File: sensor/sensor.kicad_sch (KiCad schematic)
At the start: 17 parts

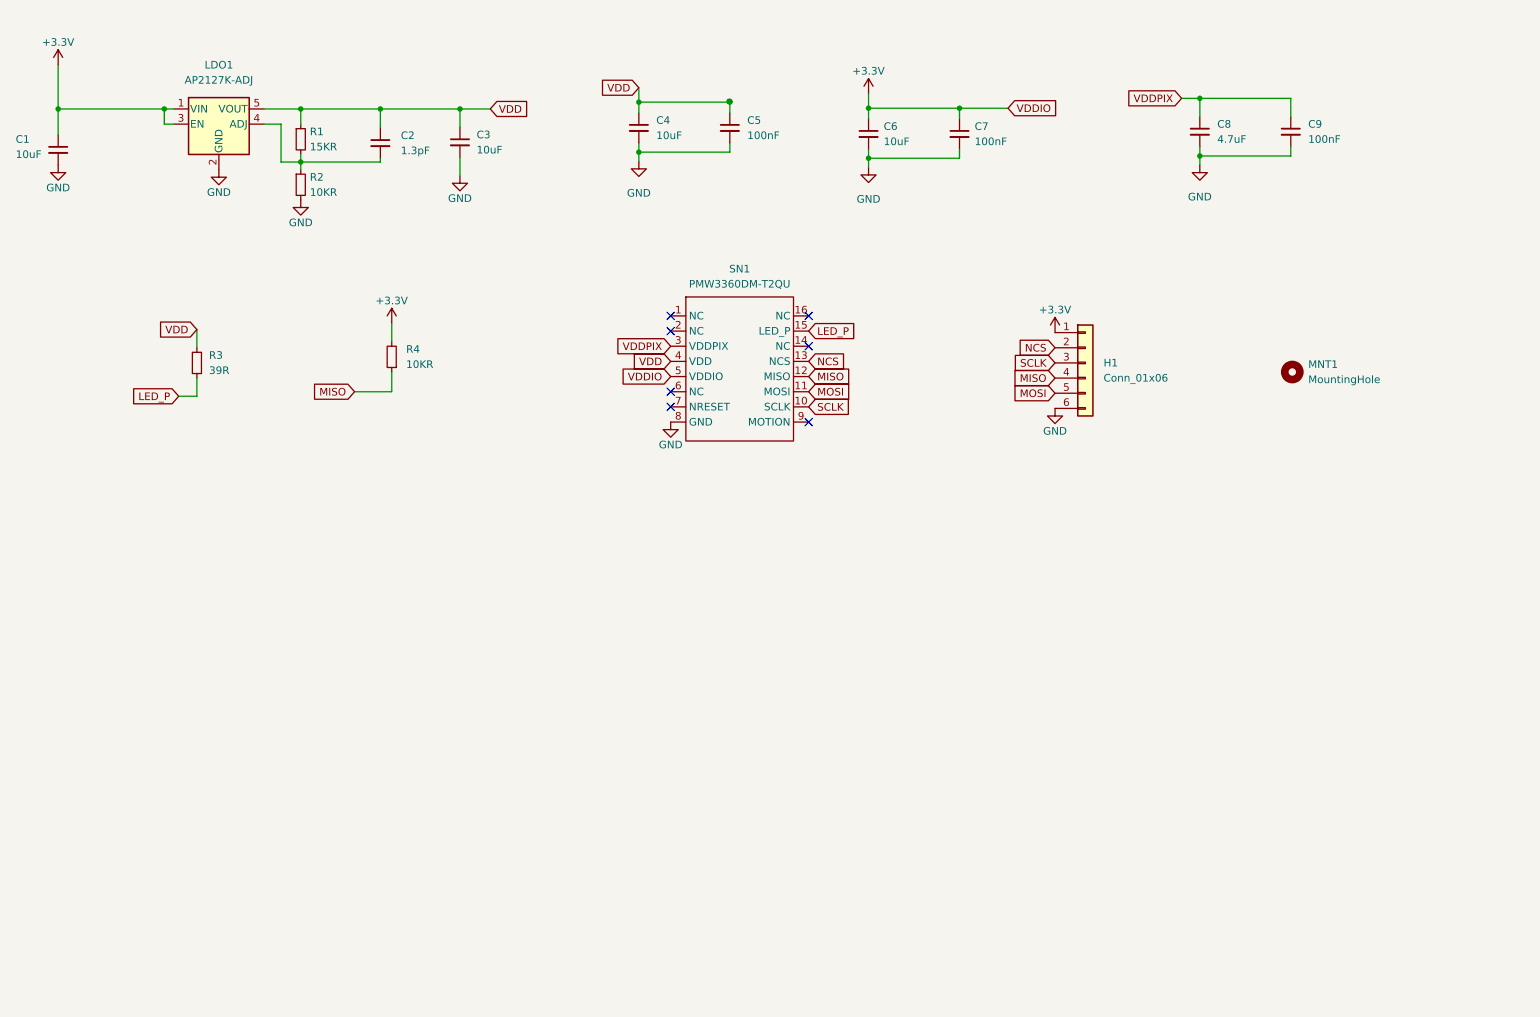
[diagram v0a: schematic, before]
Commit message: update sensor and stick, add trigger project
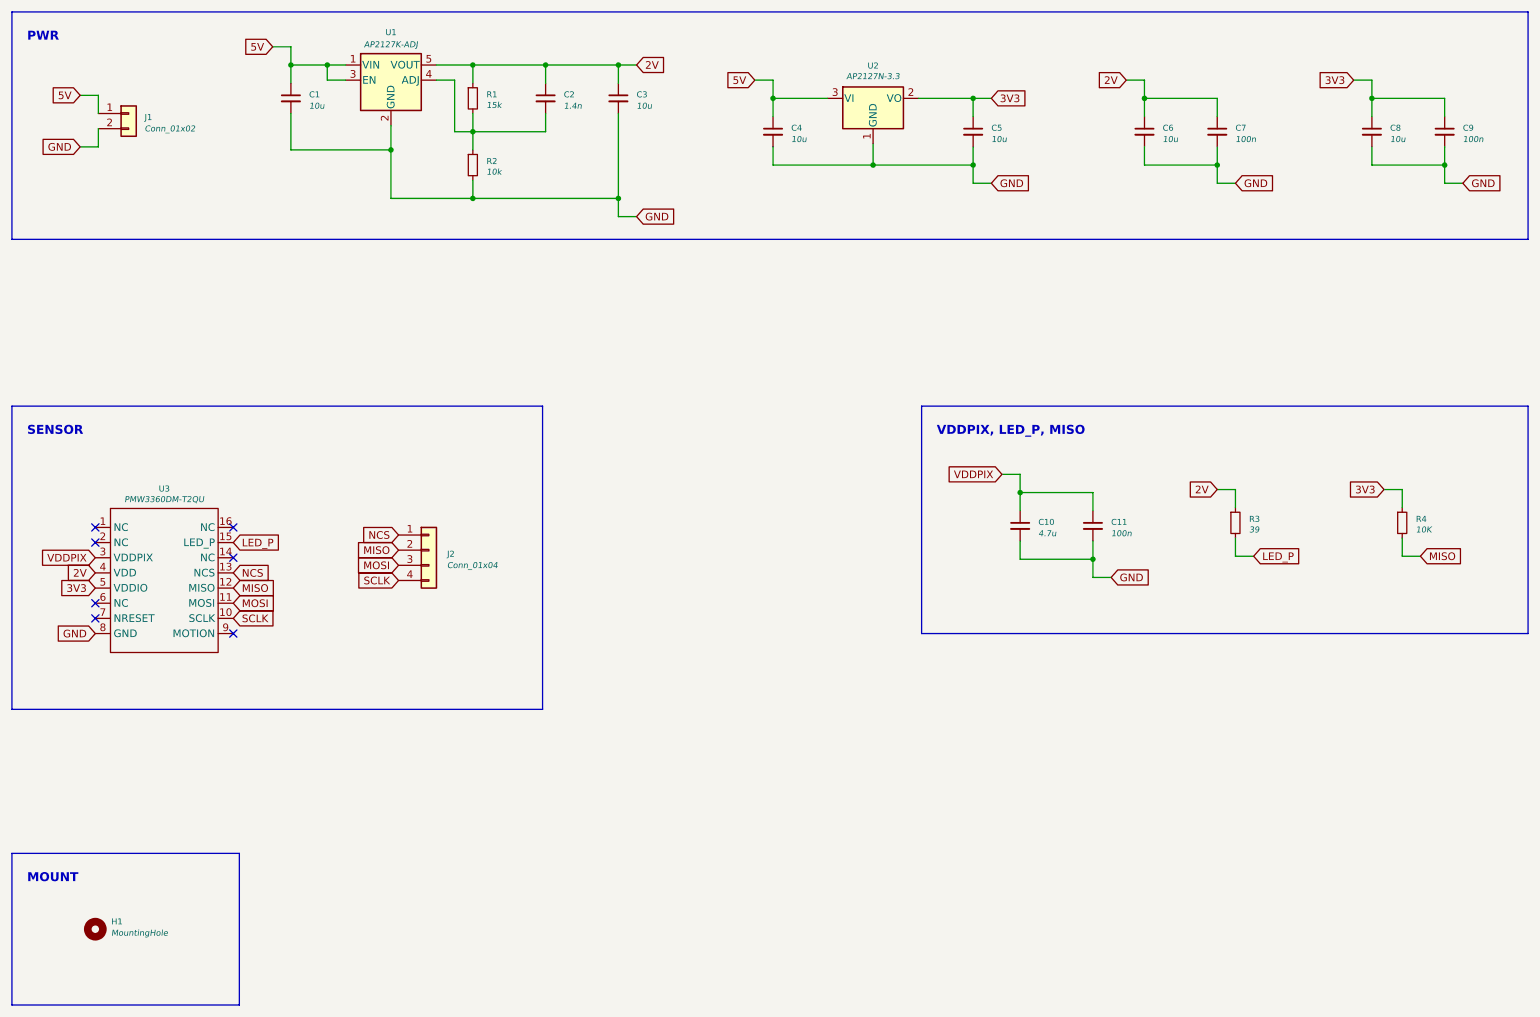
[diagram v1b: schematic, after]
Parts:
- removed H1: Conn_01x06, Connector_Molex:Molex_PicoBlade_53047-0610_1x06_P1.25mm_Vertical, symbol Connector_Generic:Conn_01x06
- removed LDO1: AP2127K-ADJ, Package_TO_SOT_SMD:SOT-23-5, symbol Regulator_Linear:AP2127K-ADJ
- added C10: 4.7u, Capacitor_SMD:C_0603_1608Metric, symbol Device:C_Small
- added C11: 100n, Capacitor_SMD:C_0603_1608Metric, symbol Device:C_Small
- added J1: Conn_01x02, klib:MOLEX_533750210-Mini-Lock-2Pin-Through-Hole, symbol Connector_Generic:Conn_01x02
- added J2: Conn_01x04, Connector_Molex:Molex_PicoBlade_53047-0410_1x04_P1.25mm_Vertical, symbol Connector_Generic:Conn_01x04
- added U1: AP2127K-ADJ, Package_TO_SOT_SMD:SOT-23-5, symbol Regulator_Linear:AP2127K-ADJ
- added U2: AP2127N-3.3, Package_TO_SOT_SMD:SOT-23, symbol Regulator_Linear:AP2127N-3.3
- C1, C3, C4, C6: value 10uF -> 10u
- C2: value 1.3pF -> 1.4n
- C5: value 100nF -> 10u
- C7, C9: value 100nF -> 100n
- C8: value 4.7uF -> 10u
- R1: value 15KR -> 15k
- R2: value 10KR -> 10k
- R3: value 39R -> 39
- R4: value 10KR -> 10K
- renumbered MNT1 to H1, SN1 to U3
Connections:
- net GND: now also C10.2, C11.2, J1.2 (Pin_2), U1.2 (GND), U2.1 (GND)
- net LED_P: now also R3.2; no longer R3.1
- net MISO: now also R4.2, J2.2 (Pin_2); no longer R4.1
- net MOSI: now also J2.3 (Pin_3)
- net NCS: now also J2.1 (Pin_1)
- net SCLK: now also J2.4 (Pin_4)
- net VDDPIX: now also C10.1, C11.1; no longer C8.1, C9.1
- net at C2.2, R1.2, R2.1: now also U1.4 (ADJ)
- removed net +3V3: C1.1, C6.1, C7.1, R4.2, U3.5 (VDDIO)
- net VDD renamed 2V
- net 2V: now also C6.1, C7.1, R3.1, U1.5 (VOUT); no longer C4.1, C5.1, R3.2
- new net 3V3: C5.1, C8.1, C9.1, R4.1, U2.2 (VO), U3.5 (VDDIO)
- new net 5V: C1.1, C4.1, J1.1 (Pin_1), U1.1 (VIN), U1.3 (EN), U2.3 (VI)
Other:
- note added: "MOUNT"
- note added: "PWR"
- note added: "SENSOR"
- note added: "VDDPIX, LED_P, MISO"
- moved on the sheet: H1, U3
